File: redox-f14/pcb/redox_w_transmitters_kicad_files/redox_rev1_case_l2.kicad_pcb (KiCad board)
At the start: 2 copper layers, 145.8 x 126.5 mm, 31 parts, among them K0 KEYSW, K1 KEYSW, K10 KEYSW, K11 KEYSW, K12 KEYSW, K13 KEYSW, K14 KEYSW, K15 KEYSW, K16 KEYSW, K2 KEYSW, K20 KEYSW, K21 KEYSW, K22 KEYSW, K23 KEYSW, K24 KEYSW, K25 KEYSW, K26 KEYSW, K3 KEYSW, K30 KEYSW, K31 KEYSW, K32 KEYSW, K33 KEYSW, K34 KEYSW, K35 KEYSW, K4 KEYSW, K42 KEYSW, K43 KEYSW, K44 KEYSW, K45 KEYSW, K5 KEYSW, K6 KEYSW

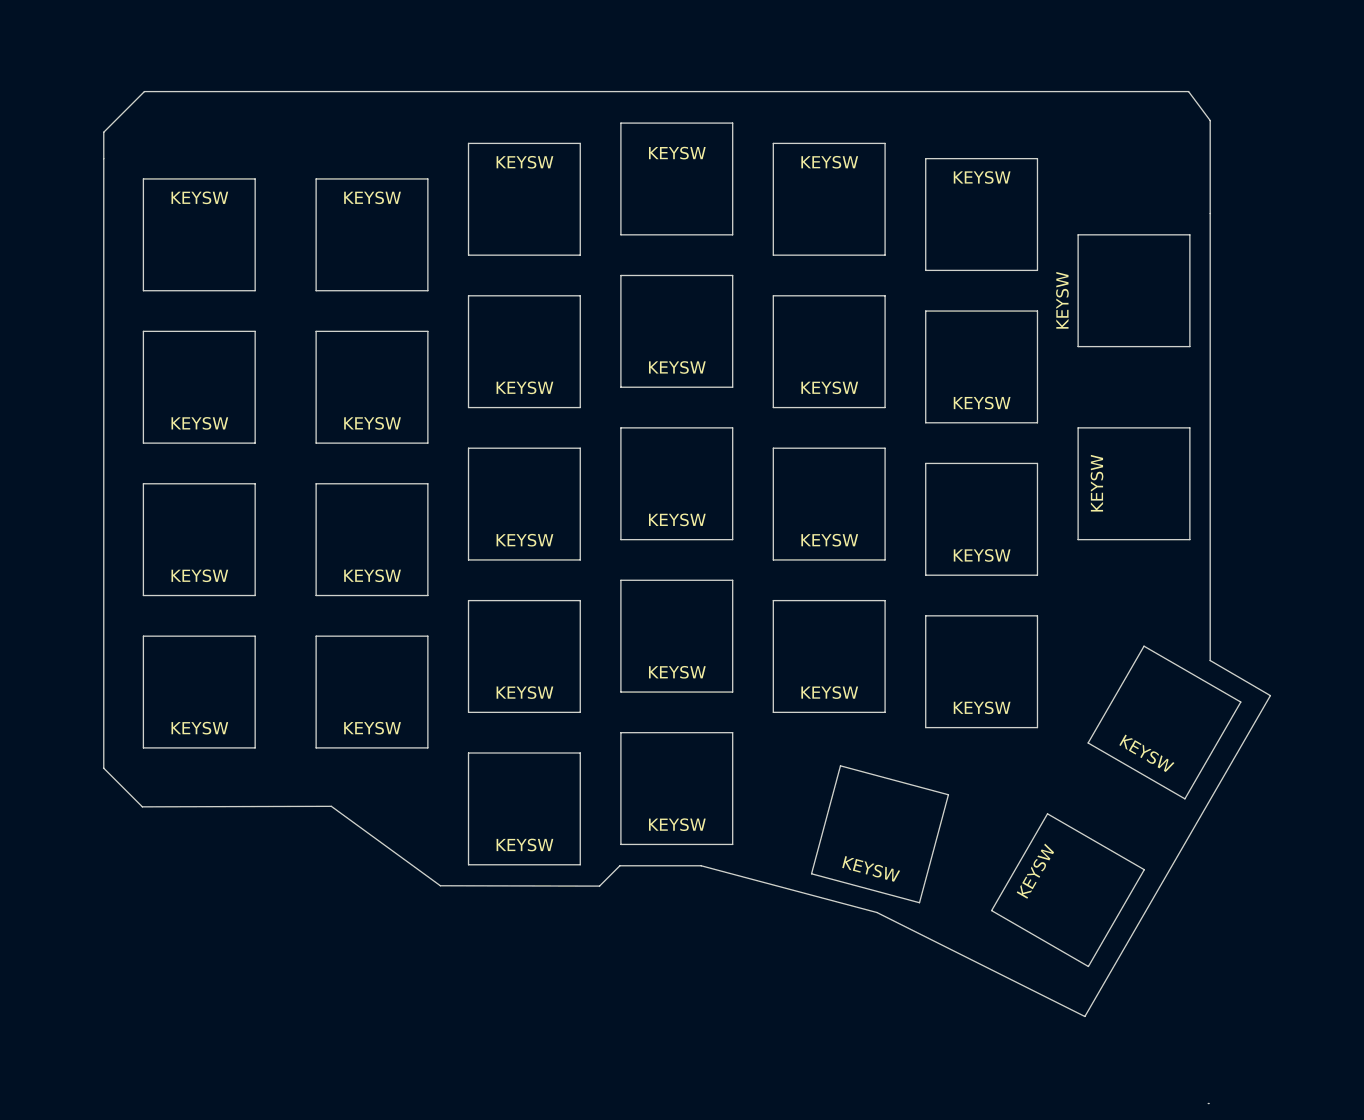
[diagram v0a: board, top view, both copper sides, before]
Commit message: add case files
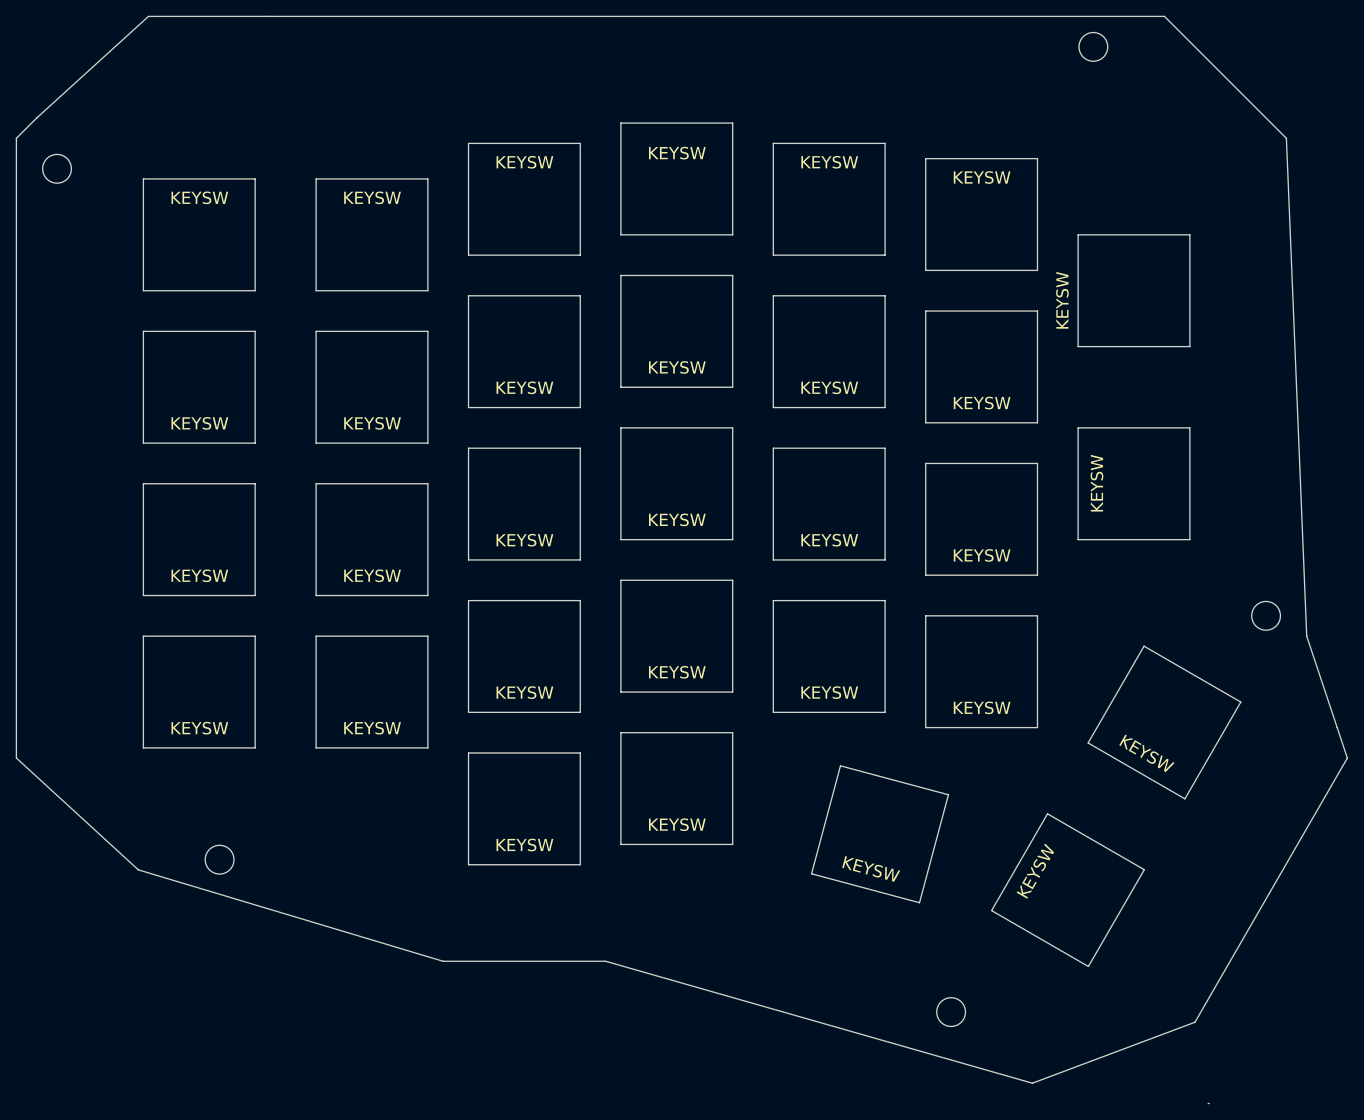
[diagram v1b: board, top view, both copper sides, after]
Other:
- board size 145.8 x 126.5 mm -> 166.4 x 135.9 mm
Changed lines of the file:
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@@
   (general
     (thickness 1.6)
-    (drawings 18)
+    (drawings 21)
     (tracks 0)
     (zones 0)
@@
     )
   )
-  (gr_line (start 215.10625 48.768) (end 217.805 52.3875) (layer Edge.Cuts) (width 0.1))
-  (gr_line (start 107.95 138.1125) (end 84.328 138.176) (layer Edge.Cuts) (width 0.1))
-  (gr_line (start 121.579395 148.040505) (end 107.95 138.1125) (layer Edge.Cuts) (width 0.1))
-  (gr_line (start 225.330156 124.273242) (end 202.142152 164.38329) (layer Edge.Cuts) (width 0.1))
-  (gr_line (start 215.10625 48.768) (end 84.582 48.768) (angle 90) (layer Edge.Cuts) (width 0.1))
-  (gr_line (start 217.805 52.3875) (end 217.805 64.008) (angle 90) (layer Edge.Cuts) (width 0.1))
-  (gr_line (start 79.502 53.848) (end 79.502 57.15) (angle 90) (layer Edge.Cuts) (width 0.1))
-  (gr_line (start 79.502 53.848) (end 84.582 48.768) (angle 90) (layer Edge.Cuts) (width 0.1))
-  (gr_line (start 154.178 145.542) (end 144.018 145.542) (angle 90) (layer Edge.Cuts) (width 0.1))
-  (gr_line (start 217.805 119.888) (end 225.330156 124.273242) (angle 90) (layer Edge.Cuts) (width 0.1))
-  (gr_line (start 217.805 64.008) (end 217.805 119.888) (angle 90) (layer Edge.Cuts) (width 0.1))
+  (gr_circle (center 203.2 43.18) (end 204.47 44.45) (layer Edge.Cuts) (width 0.1))
+  (gr_circle (center 73.66 58.42) (end 74.93 59.69) (layer Edge.Cuts) (width 0.1))
+  (gr_circle (center 93.98 144.78) (end 95.25 146.05) (layer Edge.Cuts) (width 0.1))
+  (gr_circle (center 185.42 163.83) (end 186.69 165.1) (layer Edge.Cuts) (width 0.1))
+  (gr_circle (center 224.79 114.3) (end 226.06 115.57) (layer Edge.Cuts) (width 0.1))
+  (gr_line (start 71.12 52.07) (end 85.09 39.37) (layer Edge.Cuts) (width 0.1))
+  (gr_line (start 68.58 54.61) (end 68.58 132.08) (layer Edge.Cuts) (width 0.1))
+  (gr_line (start 71.12 52.07) (end 68.58 54.61) (layer Edge.Cuts) (width 0.1))
+  (gr_line (start 83.82 146.05) (end 68.58 132.08) (layer Edge.Cuts) (width 0.1))
+  (gr_line (start 121.92 157.48) (end 83.82 146.05) (layer Edge.Cuts) (width 0.1))
+  (gr_line (start 142.24 157.48) (end 121.92 157.48) (layer Edge.Cuts) (width 0.1))
+  (gr_line (start 195.58 172.72) (end 142.24 157.48) (layer Edge.Cuts) (width 0.1))
+  (gr_line (start 215.9 165.1) (end 195.58 172.72) (layer Edge.Cuts) (width 0.1))
+  (gr_line (start 234.95 132.08) (end 215.9 165.1) (layer Edge.Cuts) (width 0.1))
+  (gr_line (start 233.68 128.27) (end 234.95 132.08) (layer Edge.Cuts) (width 0.1))
+  (gr_line (start 229.87 116.84) (end 233.68 128.27) (layer Edge.Cuts) (width 0.1))
+  (gr_line (start 227.33 54.61) (end 229.87 116.84) (layer Edge.Cuts) (width 0.1))
+  (gr_line (start 212.09 39.37) (end 227.33 54.61) (layer Edge.Cuts) (width 0.1))
+  (gr_line (start 100.33 39.37) (end 212.09 39.37) (layer Edge.Cuts) (width 0.1))
+  (gr_line (start 85.09 39.37) (end 100.33 39.37) (layer Edge.Cuts) (width 0.1))
   (gr_line (start 217.551 175.26) (end 217.678 175.26) (angle 90) (layer Edge.Cuts) (width 0.1))
-  (gr_line (start 176.149 151.384) (end 154.178 145.542) (angle 90) (layer Edge.Cuts) (width 0.1))
-  (gr_line (start 202.142152 164.38329) (end 176.149 151.384) (angle 90) (layer Edge.Cuts) (width 0.1))
-  (gr_line (start 141.478 148.082) (end 144.018 145.542) (angle 90) (layer Edge.Cuts) (width 0.1))
-  (gr_line (start 121.579395 148.040505) (end 141.478 148.082) (angle 90) (layer Edge.Cuts) (width 0.1))
-  (gr_line (start 79.502 133.35) (end 84.328 138.176) (angle 90) (layer Edge.Cuts) (width 0.1))
-  (gr_line (start 79.502 57.15) (end 79.502 133.35) (angle 90) (layer Edge.Cuts) (width 0.1))
 )
